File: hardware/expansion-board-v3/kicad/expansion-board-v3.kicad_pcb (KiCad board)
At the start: 6 copper layers, 100 x 62 mm, 157 parts, among them J1 PinHeader_2x20_P2.54mm_Vertic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, J2 U.FL_Hirose_U.FL-R-SMT-1_Vert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, J4 USB_C_Receptacle_HRO_TYPE-C-3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, J5 U.FL_Hirose_U.FL-R-SMT-1_Vert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, J6 U.FL_Hirose_U.FL-R-SMT-1_Vert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, J7 U.FL_Hirose_U.FL-R-SMT-1_Vert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, J8 U.FL_Hirose_U.FL-R-SMT-1_Vert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, Q2 SOT-23, Q3 SOT-23, Q4 SOT-23, Q5 SOT-23, SW1 SolderJumper-2_P1.3mm_Open_Pa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, SW2 SolderJumper-2_P1.3mm_Open_Pa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, U1 SOT-23-5, U10 QFN-48-1EP_7x7mm_P0.5mm_EP5.1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, U11 DFN-8-1EP_2x2mm_P0.5mm_EP0.86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, U12 SOT-363_SC-70-6, U13 AD8319_LFCSP-8-EP, U14 MSOP-8_3x3mm_P0.65mm, U15 SOT-23-6, U16 SOT-363_SC-70-6, U17 SOT-363_SC-70-6, U2 SOT-23-5, U3 SOT-23-5, U4 BNO085_LGA-28, U5 BMP388_LGA-10, U6 LGA-16_3x3mm_P0.5mm, U7 ATGM336H_LCC-18, U8 QFN-56-1EP_7x7mm_P0.4mm_EP3.2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, U9 SOIC-8_5.3x5.3mm_P1.27mm, Y1 Crystal_SMD_3225-4Pin_3.2x2.5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, Y2 Crystal_SMD_3225-4Pin_3.2x2.5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, Y3 Crystal_SMD_3215-2Pin_3.2x1.5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

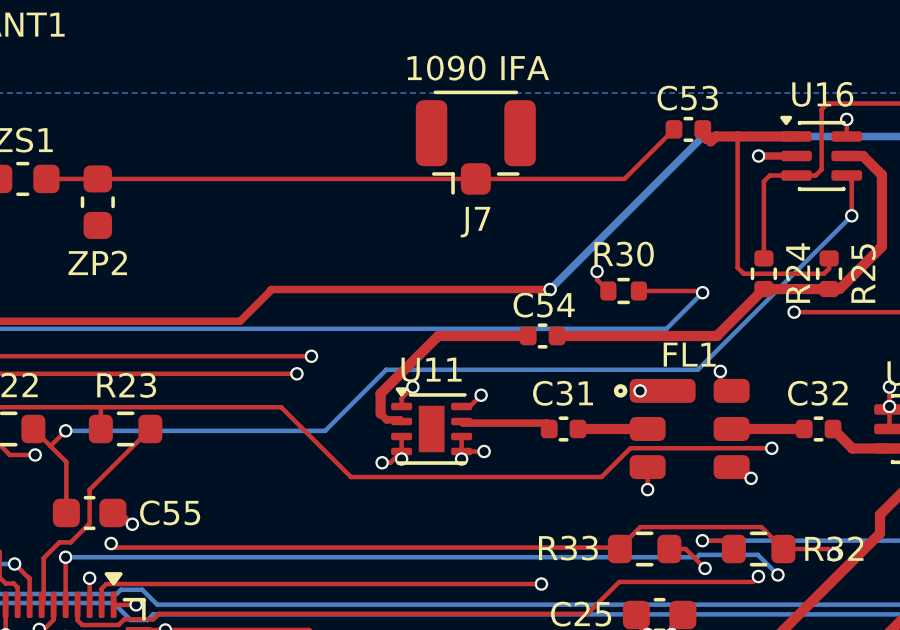
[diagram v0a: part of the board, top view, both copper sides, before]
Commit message: fix(v3): correct QPL9547 bias and release V3.8
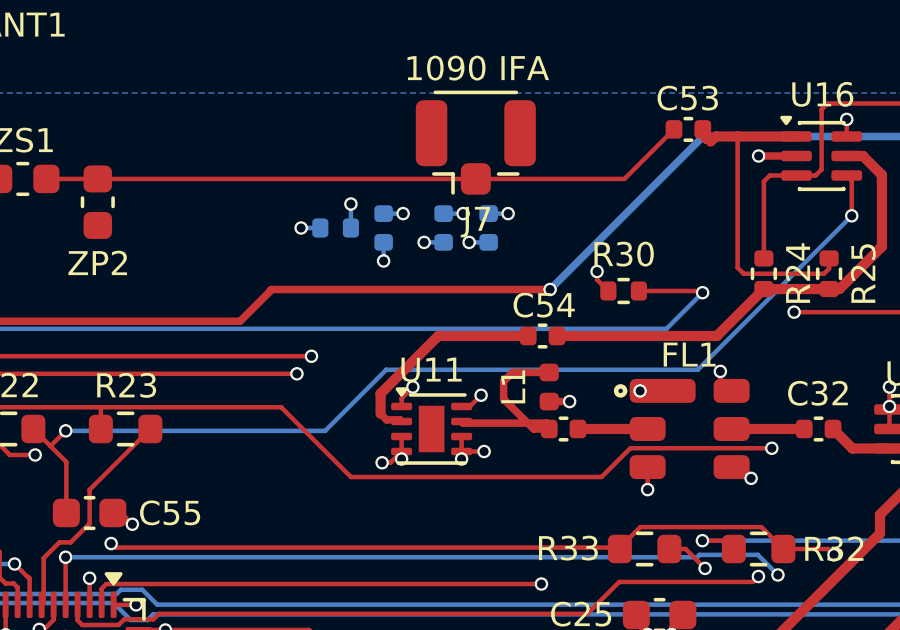
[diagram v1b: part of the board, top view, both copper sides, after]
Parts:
- added C21: C_0402_1005Metric, C_0402_1005Metric, B.Cu at (100.0, 64.5)
- added C36: C_0402_1005Metric, C_0402_1005Metric, B.Cu at (102.0, 64.5)
- added C48: C_0402_1005Metric, C_0402_1005Metric, B.Cu at (103.5, 64.5)
- added L1: L_0402_1005Metric, L_0402_1005Metric, F.Cu at (105.5, 69.8)
- added R11: R_0402_1005Metric, R_0402_1005Metric, B.Cu at (98.4, 64.5)
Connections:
- U11 pad 1: 3V3_RF -> LNA1_VBIAS
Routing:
- net 3V3_RF: track 67.2 -> 80.9 mm, vias 16 -> 19
- net LNA1_VBIAS: track 0.00 -> 9.87 mm, vias 0 -> 3
- net LNA1_OUT: track 3.10 -> 7.26 mm
- net GND: track 97.3 -> 99.2 mm, vias 132 -> 135
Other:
- board text added: "V3.8 2026-08"
- board text removed: "V3.7 2026-08"

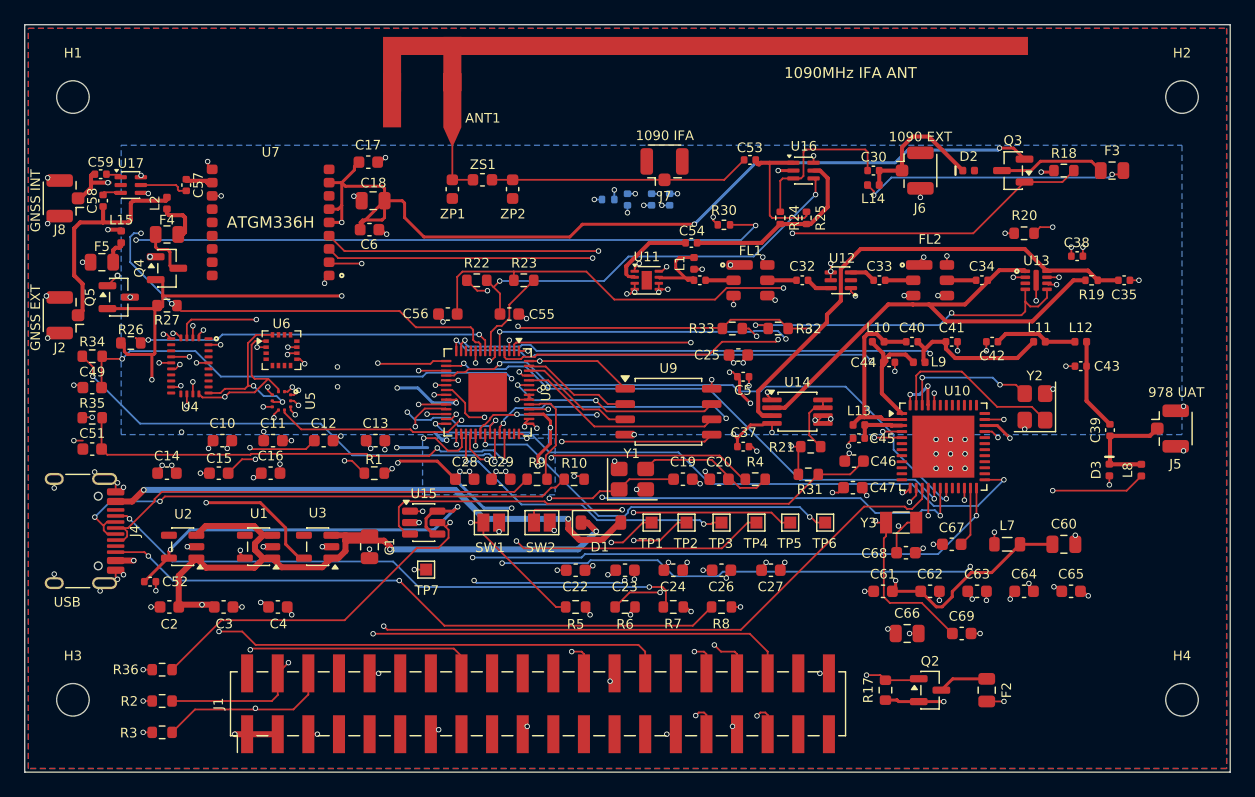
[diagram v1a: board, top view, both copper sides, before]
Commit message: feat(v3): seal V3.9 — full reroute, silkscreen, and fabrication package
Completes the V3.9 backport. The board was fully rerouted with freerouting
(8 passes, 53->16 unrouted) after the previous state turned out to be
unroutable by hand - what was left of the V3.8 routing after ripping out
176 conflicting segments was a half-connected mess. Owner finished the
remaining nets manually; the last three RF connections and the IFA feed
were closed here.

Fixes seven tool-chain defects found while sealing, most of which had been
silently corrupting the rebuild chain:

  fix_eco_silk_v38.py    pushed five designators back to the Fab layer on
                         every rebuild, undoing hand placement - and Fab
                         means they are not printed on the board at all,
                         so the V3.8 boards shipped without them. Retired.
  rebuild.sh:66          hard-coded a python path that does not exist here,
                         so the chain aborted before top_keepout_v3.py and
                         the two ANT1090_* keepouts were never rebuilt
  gen_pcb.py             FootprintLoad returns a footprint with no library
                         name, so every fpid on the board was bare and
                         schematic parity silently did not run at all
                         (reported 0 while the real count was 196)
  gen_polarity_marks.py  the outer footprint loop had no list() snapshot;
                         removing the pin-1 dot invalidated the SWIG
                         iterator. The original comment warned about this
                         and I dismissed it - it was right
  route_rf.py, stitch.py copper-fill assertions counted keepouts in the
                         denominator, reporting "not fully filled" when all
                         seven pours were fine
  gerber.sh              exported Gerber X2, which JLCPCB does not accept;
                         packed drl_map and gbrjob as if they were layers;
            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
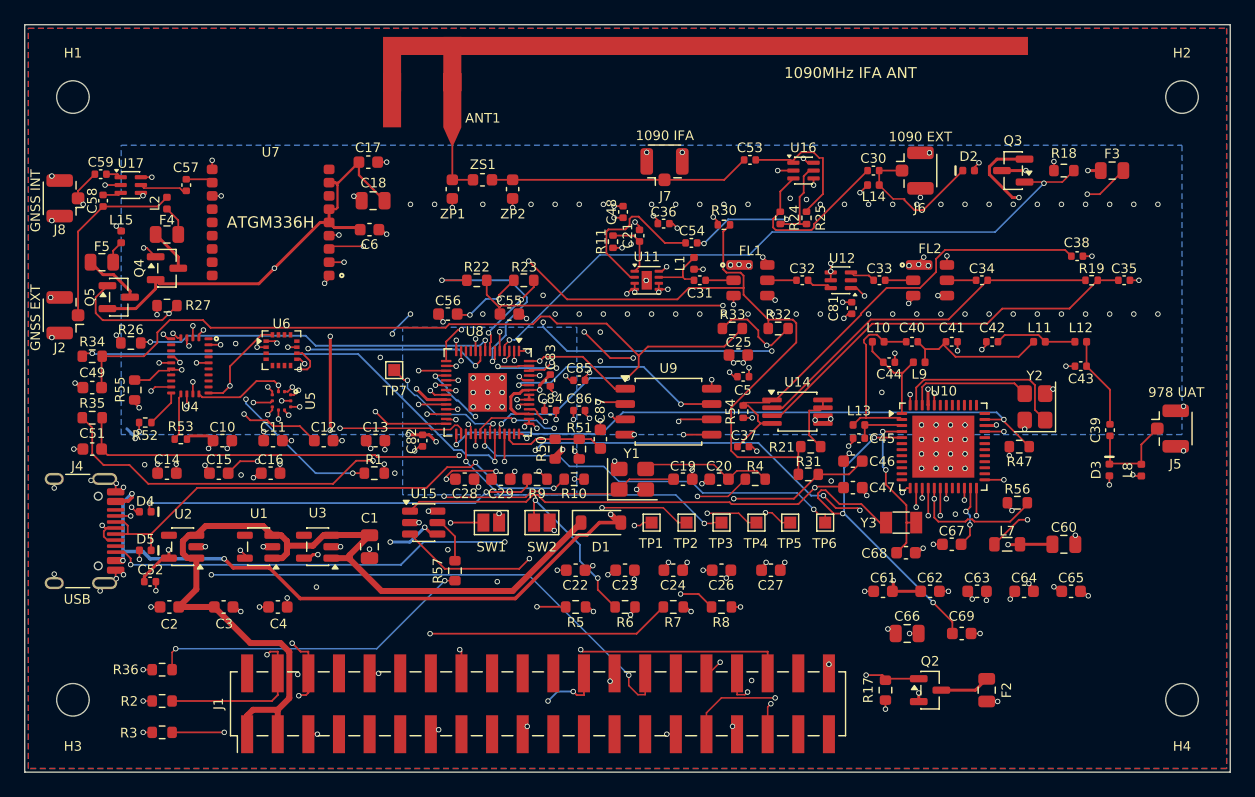
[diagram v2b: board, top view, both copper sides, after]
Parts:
- removed R20: R_0603_1608Metric, R_0603_1608Metric
- removed U13: AD8319_LFCSP-8-EP, AD8319_LFCSP-8-EP
- added C81: 470pF C0G, Capacitor_SMD:C_0402_1005Metric, F.Cu at (118.6, 73.5)
- added C82: 100nF, Capacitor_SMD:C_0402_1005Metric, F.Cu at (83.0, 84.5)
- added C83: 100nF, Capacitor_SMD:C_0402_1005Metric, F.Cu at (93.6, 79.5)
- added C84: 1uF, Capacitor_SMD:C_0402_1005Metric, F.Cu at (93.6, 82.0)
- added C85: 100nF, Capacitor_SMD:C_0402_1005Metric, F.Cu at (96.0, 79.5)
- added C86: 100nF, Capacitor_SMD:C_0402_1005Metric, F.Cu at (96.0, 82.0)
- added C87: 10nF C0G, Capacitor_SMD:C_0603_1608Metric, F.Cu at (97.8, 84.4)
- added D4: TPESD8L3.3 0.3pFtyp 0.5pFmax, Diode_SMD:D_0402_1005Metric, F.Cu at (60.0, 90.4)
- added D5: TPESD8L3.3 0.3pFtyp 0.5pFmax, Diode_SMD:D_0402_1005Metric, F.Cu at (60.0, 93.6)
- added R47: 10k, Resistor_SMD:R_0603_1608Metric, F.Cu at (132.5, 85.0)
- added R50: 10k, Resistor_SMD:R_0603_1608Metric, F.Cu at (94.0, 85.2)
- added R51: 10k, Resistor_SMD:R_0603_1608Metric, F.Cu at (96.0, 85.2)
- added R52: 10k, Resistor_SMD:R_0402_1005Metric, F.Cu at (60.0, 83.0)
- added R53: 10k, Resistor_SMD:R_0402_1005Metric, F.Cu at (63.0, 84.4)
- added R54: 10R, Resistor_SMD:R_0402_1005Metric, F.Cu at (109.6, 82.1)
- added R55: 10k, Resistor_SMD:R_0603_1608Metric, F.Cu at (59.1, 80.3)
- added R56: 10k, Resistor_SMD:R_0603_1608Metric, F.Cu at (132.3, 89.7)
- added R57: 33R, Resistor_SMD:R_0603_1608Metric, F.Cu at (85.7, 95.3)
- ANT1: value ANT_IFA_1090MHz -> IFA_1090; footprint ANT_IFA_1090MHz -> expansion-board-v3:ANT_IFA_1090MHz
- C1, C18: value C_0805_2012Metric -> 10uF; footprint C_0805_2012Metric -> Capacitor_SMD:C_0805_2012Metric
- C10, C11, C12, C13, C14, C16, C17, C22, C23, C24, C25, C26, C27, C49, C61, C62, C63, C64, C65: value C_0603_1608Metric -> 100nF; footprint C_0603_1608Metric -> Capacitor_SMD:C_0603_1608Metric
- C15: value C_0603_1608Metric -> 4.7uF; footprint C_0603_1608Metric -> Capacitor_SMD:C_0603_1608Metric
- C19, C20: value C_0603_1608Metric -> 15pF C0G; footprint C_0603_1608Metric -> Capacitor_SMD:C_0603_1608Metric
- C2, C28, C29, C3, C4, C6, C67: value C_0603_1608Metric -> 1uF; footprint C_0603_1608Metric -> Capacitor_SMD:C_0603_1608Metric
- C21, C36: value C_0402_1005Metric -> 100pF; footprint C_0402_1005Metric -> Capacitor_SMD:C_0402_1005Metric; moved to F.Cu
- C30, C38, C39, C45, C53, C54, C57, C58, C59: value C_0402_1005Metric -> 100pF; footprint C_0402_1005Metric -> Capacitor_SMD:C_0402_1005Metric
- C31, C32, C33, C34, C35: value C_0402_1005Metric -> 100pF C0G; footprint C_0402_1005Metric -> Capacitor_SMD:C_0402_1005Metric
- C37, C52: value C_0402_1005Metric -> 100nF; footprint C_0402_1005Metric -> Capacitor_SMD:C_0402_1005Metric
- C40, C44: value C_0402_1005Metric -> 3.6pF; footprint C_0402_1005Metric -> Capacitor_SMD:C_0402_1005Metric
- C41: value C_0402_1005Metric -> 2.7pF; footprint C_0402_1005Metric -> Capacitor_SMD:C_0402_1005Metric
- C42: value C_0402_1005Metric -> 6.2pF; footprint C_0402_1005Metric -> Capacitor_SMD:C_0402_1005Metric
- C43: value C_0402_1005Metric -> 3pF; footprint C_0402_1005Metric -> Capacitor_SMD:C_0402_1005Metric
- C46: value C_0603_1608Metric -> 3pF; footprint C_0603_1608Metric -> Capacitor_SMD:C_0603_1608Metric
- C47: value C_0603_1608Metric -> 200pF; footprint C_0603_1608Metric -> Capacitor_SMD:C_0603_1608Metric
- C48: value C_0402_1005Metric -> 1uF; footprint C_0402_1005Metric -> Capacitor_SMD:C_0402_1005Metric; moved to F.Cu
- C5: value C_0402_1005Metric -> 1uF; footprint C_0402_1005Metric -> Capacitor_SMD:C_0402_1005Metric
- C51: value C_0603_1608Metric -> 1nF; footprint C_0603_1608Metric -> Capacitor_SMD:C_0603_1608Metric
- C55, C56: value C_0603_1608Metric -> 100pF; footprint C_0603_1608Metric -> Capacitor_SMD:C_0603_1608Metric
- C60, C66: value C_0805_2012Metric -> 22uF; footprint C_0805_2012Metric -> Capacitor_SMD:C_0805_2012Metric
- C68, C69: value C_0603_1608Metric -> 18pF; footprint C_0603_1608Metric -> Capacitor_SMD:C_0603_1608Metric
- D1: value D_SOD-123 -> B5819W; footprint D_SOD-123 -> Diode_SMD:D_SOD-123
- D2, D3: value D_0402_1005Metric -> TPESD8L3.3 0.3pFtyp 0.5pFmax; footprint D_0402_1005Metric -> Diode_SMD:D_0402_1005Metric
- F2, F3, F4, F5: value Fuse_0805_2012Metric -> 6V/200mA; footprint Fuse_0805_2012Metric -> Fuse:Fuse_0805_2012Metric
- FL1, FL2: value TA0970A_SMD3838-6 -> TA0970A; footprint TA0970A_SMD3838-6 -> expansion-board-v3:TA0970A_SMD3838-6
- J1: value PinHeader_2x20_P2.54mm_Vertical_SMD -> J3_HAT_2x20_SMD排针; footprint PinHeader_2x20_P2.54mm_Vertical_SMD -> Connector_PinHeader_2.54mm:PinHeader_2x20_P2.54mm_Vertical_SMD
- J2: value U.FL_Hirose_U.FL-R-SMT-1_Vertical -> U.FL_GNSS_EXT(经尾线转SMA); footprint U.FL_Hirose_U.FL-R-SMT-1_Vertical -> Connector_Coaxial:U.FL_Hirose_U.FL-R-SMT-1_Vertical
- J4: value USB_C_Receptacle_HRO_TYPE-C-31-M-12 -> USB-C_16P; footprint USB_C_Receptacle_HRO_TYPE-C-31-M-12 -> Connector_USB:USB_C_Receptacle_HRO_TYPE-C-31-M-12
- J5: value U.FL_Hirose_U.FL-R-SMT-1_Vertical -> U.FL_978; footprint U.FL_Hirose_U.FL-R-SMT-1_Vertical -> Connector_Coaxial:U.FL_Hirose_U.FL-R-SMT-1_Vertical
- J6: value U.FL_Hirose_U.FL-R-SMT-1_Vertical -> U.FL_1090_EXT(经尾线转SMA); footprint U.FL_Hirose_U.FL-R-SMT-1_Vertical -> Connector_Coaxial:U.FL_Hirose_U.FL-R-SMT-1_Vertical
- J7: value U.FL_Hirose_U.FL-R-SMT-1_Vertical -> U.FL_IFA_TEST(π后调试口); footprint U.FL_Hirose_U.FL-R-SMT-1_Vertical -> Connector_Coaxial:U.FL_Hirose_U.FL-R-SMT-1_Vertical
- J8: value U.FL_Hirose_U.FL-R-SMT-1_Vertical -> U.FL→内置patch; footprint U.FL_Hirose_U.FL-R-SMT-1_Vertical -> Connector_Coaxial:U.FL_Hirose_U.FL-R-SMT-1_Vertical
- L1: value L_0402_1005Metric -> 18nH 0402CS-18NXGRW; footprint L_0402_1005Metric -> Inductor_SMD:L_0402_1005Metric
- L10: value L_0402_1005Metric -> 27nH; footprint L_0402_1005Metric -> Inductor_SMD:L_0402_1005Metric
- L11, L12: value L_0402_1005Metric -> 6.8nH; footprint L_0402_1005Metric -> Inductor_SMD:L_0402_1005Metric
- L13, L9: value L_0402_1005Metric -> 7.5nH; footprint L_0402_1005Metric -> Inductor_SMD:L_0402_1005Metric
- L14, L8: value L_0402_1005Metric -> 100nH; footprint L_0402_1005Metric -> Inductor_SMD:L_0402_1005Metric
- L15, L2: value L_0402_1005Metric -> 33nH; footprint L_0402_1005Metric -> Inductor_SMD:L_0402_1005Metric
- L7: value L_0805_2012Metric -> 6.8uH; footprint L_0805_2012Metric -> Inductor_SMD:L_0805_2012Metric
- Q2, Q3, Q4, Q5: value SOT-23 -> AO3401A; footprint SOT-23 -> Package_TO_SOT_SMD:SOT-23
- R1, R17, R18, R26, R27, R32, R34, R35, R5, R6: value R_0603_1608Metric -> 10k; footprint R_0603_1608Metric -> Resistor_SMD:R_0603_1608Metric
- R10, R9: value R_0603_1608Metric -> 27R; footprint R_0603_1608Metric -> Resistor_SMD:R_0603_1608Metric
- R11: value R_0402_1005Metric -> 3.32k; footprint R_0402_1005Metric -> Resistor_SMD:R_0402_1005Metric; moved to F.Cu
- R19: value R_0402_1005Metric -> 52.3R; footprint R_0402_1005Metric -> Resistor_SMD:R_0402_1005Metric
- R2, R3: value R_0603_1608Metric -> 4.7k; footprint R_0603_1608Metric -> Resistor_SMD:R_0603_1608Metric
- R21, R22, R23: value R_0603_1608Metric -> 0R; footprint R_0603_1608Metric -> Resistor_SMD:R_0603_1608Metric
- R24: value R_0402_1005Metric -> 0R DNP(旁路外接); footprint R_0402_1005Metric -> Resistor_SMD:R_0402_1005Metric
- R25: value R_0402_1005Metric -> 0R DNP(旁路板载); footprint R_0402_1005Metric -> Resistor_SMD:R_0402_1005Metric
- R30: value R_0402_1005Metric -> 1k DNP; footprint R_0402_1005Metric -> Resistor_SMD:R_0402_1005Metric
- R31, R4: value R_0603_1608Metric -> 1k; footprint R_0603_1608Metric -> Resistor_SMD:R_0603_1608Metric
- R33: value R_0603_1608Metric -> 100k; footprint R_0603_1608Metric -> Resistor_SMD:R_0603_1608Metric
- R36: value R_0603_1608Metric -> 1k DNP; footprint R_0603_1608Metric -> Resistor_SMD:R_0603_1608Metric
- R7, R8: value R_0603_1608Metric -> 5.1k; footprint R_0603_1608Metric -> Resistor_SMD:R_0603_1608Metric
- SW1: value SolderJumper-2_P1.3mm_Open_Pad1.0x1.5mm -> RESET短接焊盘; footprint SolderJumper-2_P1.3mm_Open_Pad1.0x1.5mm -> Jumper:SolderJumper-2_P1.3mm_Open_Pad1.0x1.5mm
- SW2: value SolderJumper-2_P1.3mm_Open_Pad1.0x1.5mm -> BOOTSEL短接焊盘; footprint SolderJumper-2_P1.3mm_Open_Pad1.0x1.5mm -> Jumper:SolderJumper-2_P1.3mm_Open_Pad1.0x1.5mm
- TP1, TP2, TP3, TP4, TP5, TP6, TP7: value TestPoint_Pad_1.0x1.0mm -> TestPoint; footprint TestPoint_Pad_1.0x1.0mm -> TestPoint:TestPoint_Pad_1.0x1.0mm
- U1: value SOT-23-5 -> ME6211C33M5; footprint SOT-23-5 -> Package_TO_SOT_SMD:SOT-23-5
- U10: value QFN-48-1EP_7x7mm_P0.5mm_EP5.15x5.15mm -> CC1312R1F3RGZR; footprint QFN-48-1EP_7x7mm_P0.5mm_EP5.15x5.15mm -> Package_DFN_QFN:QFN-48-1EP_7x7mm_P0.5mm_EP5.15x5.15mm
- U11: value DFN-8-1EP_2x2mm_P0.5mm_EP0.86x1.55mm -> QPL9547TR7; footprint DFN-8-1EP_2x2mm_P0.5mm_EP0.86x1.55mm -> Package_DFN_QFN:DFN-8-1EP_2x2mm_P0.5mm_EP0.86x1.55mm
- U12: value SOT-363_SC-70-6 -> BGA2817; footprint SOT-363_SC-70-6 -> Package_TO_SOT_SMD:SOT-363_SC-70-6
- U14: value MSOP-8_3x3mm_P0.65mm -> AD8313ARMZ; footprint MSOP-8_3x3mm_P0.65mm -> Package_SO:MSOP-8_3x3mm_P0.65mm
- U15: value SOT-23-6 -> TLV3501(TOKMAS); footprint SOT-23-6 -> Package_TO_SOT_SMD:SOT-23-6
- U16, U17: value SOT-363_SC-70-6 -> XA17-G4K; footprint SOT-363_SC-70-6 -> Package_TO_SOT_SMD:SOT-363_SC-70-6
- U2, U3: value SOT-23-5 -> TPS7A2033PDBVR; footprint SOT-23-5 -> Package_TO_SOT_SMD:SOT-23-5
- U4: value BNO085_LGA-28 -> BNO085; footprint BNO085_LGA-28 -> expansion-board-v3:BNO085_LGA-28
- U5: value BMP388_LGA-10 -> BMP388; footprint BMP388_LGA-10 -> expansion-board-v3:BMP388_LGA-10
- U6: value LGA-16_3x3mm_P0.5mm -> QMC5883P; footprint LGA-16_3x3mm_P0.5mm -> Package_LGA:LGA-16_3x3mm_P0.5mm
- U7: value ATGM336H_LCC-18 -> ATGM336H-6N-74; footprint ATGM336H_LCC-18 -> expansion-board-v3:ATGM336H_LCC-18
- U8: value QFN-56-1EP_7x7mm_P0.4mm_EP3.2x3.2mm -> RP2040; footprint QFN-56-1EP_7x7mm_P0.4mm_EP3.2x3.2mm -> Package_DFN_QFN:QFN-56-1EP_7x7mm_P0.4mm_EP3.2x3.2mm
- U9: value SOIC-8_5.3x5.3mm_P1.27mm -> W25Q128JVSIQ; footprint SOIC-8_5.3x5.3mm_P1.27mm -> Package_SO:SOIC-8_5.3x5.3mm_P1.27mm
- Y1: value Crystal_SMD_3225-4Pin_3.2x2.5mm -> 12MHz CL=10pF ABM8-272-T3; footprint Crystal_SMD_3225-4Pin_3.2x2.5mm -> Crystal:Crystal_SMD_3225-4Pin_3.2x2.5mm
- Y2: value Crystal_SMD_3225-4Pin_3.2x2.5mm -> 48MHz ABM8W-7pF; footprint Crystal_SMD_3225-4Pin_3.2x2.5mm -> Crystal:Crystal_SMD_3225-4Pin_3.2x2.5mm
- Y3: value Crystal_SMD_3215-2Pin_3.2x1.5mm -> 32.768kHz FC-135; footprint Crystal_SMD_3215-2Pin_3.2x1.5mm -> Crystal:Crystal_SMD_3215-2Pin_3.2x1.5mm
- ZP1: value C_0603_1608Metric -> DNP 并-天线侧; footprint C_0603_1608Metric -> Capacitor_SMD:C_0603_1608Metric
- ZP2: value C_0603_1608Metric -> DNP 并-电台侧; footprint C_0603_1608Metric -> Capacitor_SMD:C_0603_1608Metric
- ZS1: value L_0603_1608Metric -> 0R 串; footprint L_0603_1608Metric -> Inductor_SMD:L_0603_1608Metric
- moved TP7 16.8 mm to (80.7, 78.7)
- moved C48 4.00 mm to (99.6, 65.5)
- moved R11 3.52 mm to (98.8, 68.0), turned to 90 degrees
- moved C21 3.16 mm to (101.0, 67.5)
- moved C36 2.24 mm to (103.0, 66.5), turned to 0 degrees
- moved C46 0.10 mm to (118.7, 86.2)
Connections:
- C37 pad 1: 3V3_RF -> AD8313_VPOS
- C38 pad 1: 3V3_RF -> AD8313_VPOS
- R17 pad 1: 3V3_GNSS -> 3V3_DIG
- R18 pad 1: 3V3_GNSS -> 3V3_DIG
- R26 pad 1: 3V3_GNSS -> 3V3_DIG
- R27 pad 1: 3V3_GNSS -> 3V3_DIG
- U14 pad 1: 3V3_RF -> AD8313_VPOS
- U14 pad 4: 3V3_RF -> AD8313_VPOS
- U15 pad 5: PULSES -> PULSES_RAW
- U15 pad 6: 3V3_RF -> GND
- U4 pad 15: unconnected-(U4-ENV_SCL-Pad15) -> BNO_ENV_SCL
- U4 pad 16: unconnected-(U4-ENV_SDA-Pad16) -> BNO_ENV_SDA
- U8 pad 40: unconnected-(U8-GPIO28/ADC2-Pad40) -> USB_VBUS_SENSE
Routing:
- net AD8313_VPOS: track 0.00 -> 39.6 mm
- net SUBG_TCKC: track 53.3 -> 88.6 mm
- net 3V3_RF: track 80.9 -> 51.2 mm, vias 19 -> 15
- net SUBG_MISO: track 78.2 -> 50.5 mm, vias 2 -> 4
- net 3V3_GNSS: track 195.5 -> 172.3 mm, vias 8 -> 4
- net RP_1V1: track 44.1 -> 22.6 mm, vias 10 -> 6
- net RF_DET_OUT: track 122.9 -> 105.2 mm, vias 6 -> 2
- net SUBG_CSN: track 46.3 -> 62.7 mm
- net SWDIO: track 39.8 -> 25.0 mm, vias 4 -> 2
- net SUBG_RESET: track 67.1 -> 52.5 mm, vias 4 -> 2
- net GND: track 99.2 -> 113.8 mm, vias 135 -> 246
- net SWCLK: track 44.2 -> 31.3 mm
- net RECOVERED_CLK: track 23.9 -> 11.4 mm, vias 3 -> 2
- net ADSB_RXD: track 41.1 -> 53.2 mm
- net PULSES: track 42.6 -> 54.6 mm, vias 2 -> 3
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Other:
- board text added: "V3.9 2026-09"
- board text removed: "V3.8 2026-08"
